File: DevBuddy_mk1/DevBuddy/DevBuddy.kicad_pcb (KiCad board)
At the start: 2 copper layers, 283 parts, among them J1 2171820001, J2 Conn_01x02_Socket, J3 Debug Conn, J4 UART_Conns, J5 PC30, J6 Conn_01x15_Pin, Q1 AO3415A, Q10 AO3415A, Q2 BC817, Q3 BC817, Q4 AO3415A, Q5 BC817, Q6 AO3415A, Q7 BC817, Q8 AO3415A, Q9 BC817, U1 RP2354B, U10 TPS62913, U11 TPS54331DDAR, U12 MCP4725xxx-xCH, U13 TPS55289RYQR, U14 MCP4725xxx-xCH, U15 NCP1117-3.3_SOT223, U16 74HC4051, U17 TPS22965NQWDSGRQ1, U18 TPS22965NQWDSGRQ1, U19 TPS22965NQWDSGRQ1, U2 74HC4051, U3 74HC4051, U4 INA190A2IDCKR, U5 TPS54331DDAR, U6 TPS54331DDAR, U7 TPS62913, U8 TPS62913, U9 TPS55289RYQR, Y1 12MHz

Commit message: PCB, initial routing of submods
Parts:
- R13, R14, R26, R27, R8, R9: footprint Resistor_SMD:R_01005_0402Metric -> Resistor_SMD:R_0402_1005Metric
- moved R46 241.5 mm to (23.4, 150.4)
- moved R35 239.7 mm to (23.4, 152.4), turned to 180 degrees
- moved R34 239.5 mm to (23.4, 149.4), turned to 180 degrees
- moved C85 237.5 mm to (23.4, 151.4), turned to 180 degrees
- moved U13 237.3 mm to (29.4, 149.4)
- moved R33 235.1 mm to (23.4, 148.4)
- moved R51 233.8 mm to (35.0, 154.7), turned to -90 degrees
- moved C83 233.4 mm to (28.2, 153.3)
- moved C93 233.0 mm to (32.6, 163.6), turned to 180 degrees
- moved R52 232.4 mm to (36.0, 154.7), turned to -90 degrees
- moved R48 231.9 mm to (36.9, 149.2), turned to 90 degrees
- moved R41 231.9 mm to (34.0, 149.2), turned to 90 degrees
- moved C81 229.2 mm to (25.1, 159.5)
- moved C87 228.6 mm to (35.4, 148.7), turned to 180 degrees
- moved C102 228.4 mm to (35.5, 153.2)
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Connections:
- R13 pad 1: Net-(U6-VSENSE) -> 12V_C_CurSense_Hi
- R13 pad 2: 12V_C_CurSense_Hi -> Net-(U6-VSENSE)
- R14 pad 1: GND -> Net-(U6-VSENSE)
- R14 pad 2: Net-(U6-VSENSE) -> GND
- R26 pad 1: Net-(U11-VSENSE) -> 12V_D_CurSense_Hi
- R26 pad 2: 12V_D_CurSense_Hi -> Net-(U11-VSENSE)
- R27 pad 1: GND -> Net-(U11-VSENSE)
- R27 pad 2: Net-(U11-VSENSE) -> GND
- R8 pad 1: Net-(U5-VSENSE) -> +3V3
- R8 pad 2: +3V3 -> Net-(U5-VSENSE)
- R9 pad 1: GND -> Net-(U5-VSENSE)
- R9 pad 2: Net-(U5-VSENSE) -> GND
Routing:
- net +3V3: track 0.00 -> 64.3 mm
- net 5V_D_CurSense_Hi: track 0.00 -> 38.3 mm
- net 5V_C_CurSense_Hi: track 0.00 -> 36.9 mm
- net 3V3_C_CurSense_Hi: track 0.00 -> 33.2 mm
- net 12V_C_CurSense_Hi: track 0.00 -> 25.0 mm
- net 12V_D_CurSense_Hi: track 0.00 -> 24.3 mm
- net /Power_Supply_2/VCC_buck: track 0.00 -> 22.5 mm, vias 0 -> 3
- net /Power_Supply_2/VCC_buck_2: track 0.00 -> 21.2 mm, vias 0 -> 2
- net Net-(U1-XIN): track 0.00 -> 16.4 mm
- net AGND: track 0.00 -> 14.6 mm
- net GND: track 0.00 -> 13.6 mm
- net /ADC_Channels/ADC_in_Hi: track 0.00 -> 11.6 mm
- net /ADC_Channels/ADC_in_Low: track 0.00 -> 10.8 mm
- net Net-(U5-BOOT): track 0.00 -> 8.64 mm, vias 0 -> 2
- net Net-(U6-BOOT): track 0.00 -> 8.60 mm, vias 0 -> 2
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- added copper zone on F.Cu, net +3V3
- added copper zone on F.Cu, net 12V_C_CurSense_Hi
- added copper zone on F.Cu, net 12V_C_CurSense_Low
- added copper zone on F.Cu, net 12V_D_CurSense_Hi
- added copper zone on F.Cu, net 12V_D_CurSense_Low
- added copper zone on F.Cu, net 3V3_C_CurSense_Hi
- added copper zone on F.Cu, net 3V3_C_CurSense_Low
- added copper zone on F.Cu, net 5V_C_CurSense_Hi
- added copper zone on F.Cu, net 5V_D_CurSense_Hi
- added copper zone on F.Cu, net GND
- added copper zone on F.Cu, net Net-(D1-K)
- added copper zone on F.Cu, net Net-(D2-K)
- added copper zone on F.Cu, net Net-(D3-K)
- added copper zone on F.Cu, net Net-(R43-Pad2)
- added copper zone on F.Cu, net Net-(R45-Pad2)
- added copper zone on F.Cu, net Net-(U10-VO)
- added copper zone on F.Cu, net Net-(U13-SW1)
- added copper zone on F.Cu, net Net-(U13-SW2)
- added copper zone on F.Cu, net Net-(U7-SW)
- added copper zone on F.Cu, net Net-(U7-VO)
- added copper zone on F.Cu, net Net-(U8-SW)
- added copper zone on F.Cu, net Net-(U8-VO)
- added copper zone on F.Cu, net Net-(U9-SW1)
- added copper zone on F.Cu, net Net-(U9-SW2)
- added copper zone on F.Cu, net VCC_CurSense_Low
- added copper zone on F.Cu, net Var_V1_CurSense_Hi
- added copper zone on F.Cu, net Var_V1_CurSense_Low
- added copper zone on F.Cu, net Var_V2_CurSense_Hi
- added copper zone on F.Cu, net Var_V2_CurSense_Low

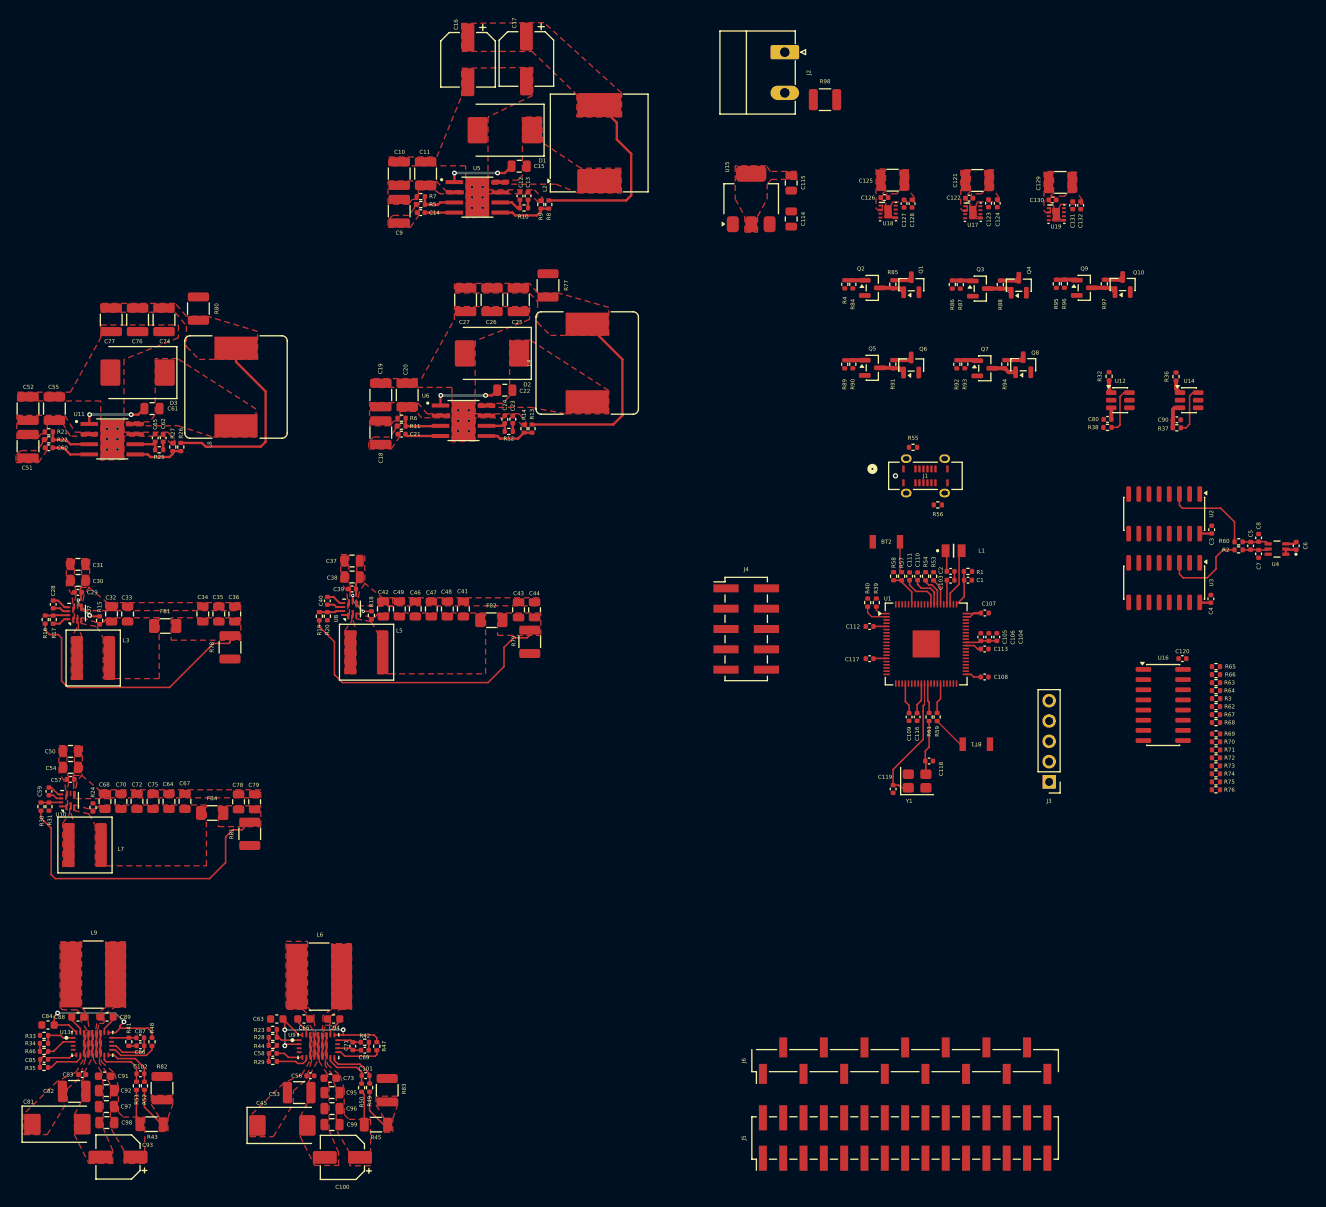
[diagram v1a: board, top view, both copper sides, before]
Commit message: PCB, first draft of PCB layout
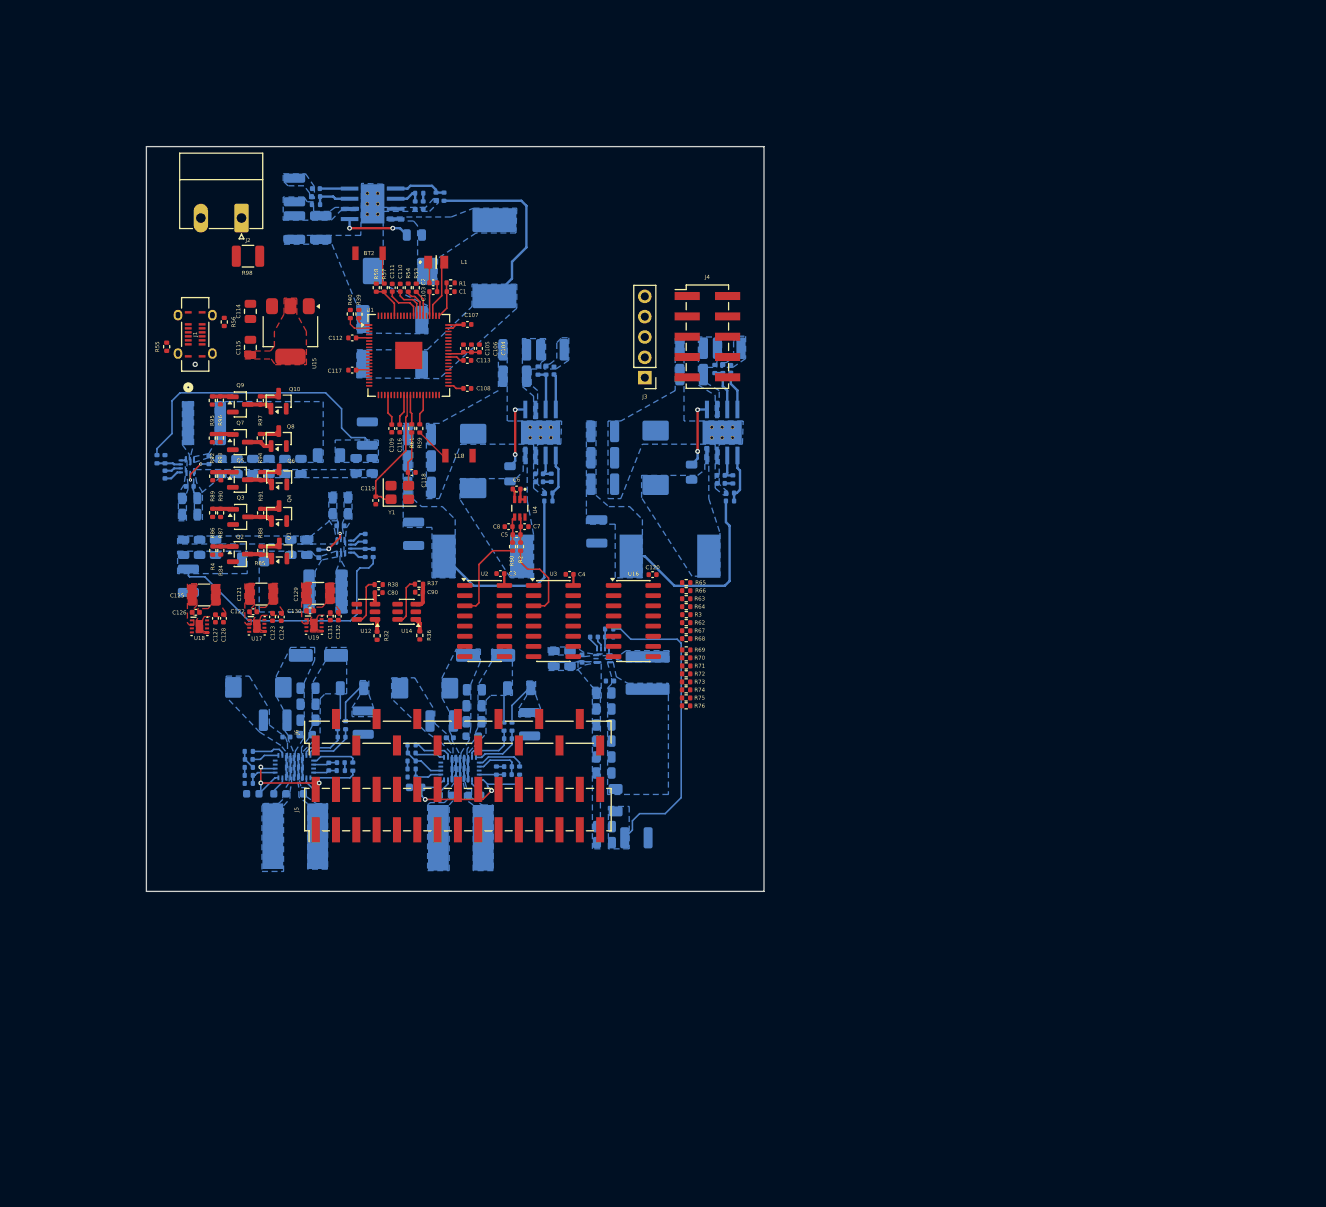
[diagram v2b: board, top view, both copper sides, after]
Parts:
- C10, C100, C101, C102, C11, C12, C13, C14, C15, C16, C17, C18, C19, C20, C21, C22, C23, C24, C25, C26, C27, C28, C29, C30, C31, C32, C33, C34, C35, C36, C37, C38, C39, C40, C41, C42, C43, C44, C45, C46, C47, C48, C49, C50, C51, C52, C53, C54, C55, C56, C57, C58, C59, C60, C61, C62, C63, C64, C65, C66, C67, C68, C69, C70, C71, C72, C73, C74, C75, C76, C77, C78, C79, C81, C82, C83, C84, C85, C86, C87, C88, C89, C9, C91, C92, C93, C94, C95, C96, C97, C98, C99, D1, D2, D3, FB1, FB2, FB4, L2, L3, L4, L5, L6, L7, L8, L9, R10, R11, R12, R13, R14, R15, R16, R17, R18, R19, R20, R21, R22, R23, R24, R25, R26, R27, R28, R29, R30, R31, R33, R34, R35, R41, R42, R43, R44, R45, R46, R47, R48, R49, R5, R50, R51, R52, R6, R7, R77, R78, R79, R8, R80, R81, R82, R83, R9, U10, U11, U13, U5, U6, U7, U8, U9: moved to B.Cu
- moved Q10 106.5 mm to (52.7, 69.1)
- moved Q9 106.5 mm to (47.9, 69.5)
- moved R95 106.5 mm to (44.4, 69.0)
- moved R96 106.5 mm to (45.4, 69.0)
- moved R97 106.5 mm to (50.4, 69.0)
- moved U19 106.1 mm to (57.2, 97.1)
- moved C129 106.1 mm to (57.7, 93.1)
- moved C130 106.1 mm to (56.7, 95.3)
- moved C131 106.1 mm to (59.2, 96.0)
- moved C132 106.1 mm to (60.2, 96.0)
- moved C121 103.4 mm to (50.6, 93.2)
- moved C123 103.4 mm to (52.0, 96.1)
- moved C124 103.4 mm to (53.1, 96.1)
- moved U17 103.4 mm to (50.0, 97.2)
- moved C122 103.4 mm to (49.5, 95.4)
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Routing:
- net 12V_C_CurSense_Hi: track 25.0 -> 24.1 mm
- added copper zone on B.Cu, net +3V3
- added copper zone on B.Cu, net 12V_C_CurSense_Hi
- added copper zone on B.Cu, net 12V_C_CurSense_Low
- added copper zone on B.Cu, net 12V_D_CurSense_Hi
- added copper zone on B.Cu, net 12V_D_CurSense_Low
- added copper zone on B.Cu, net 3V3_C_CurSense_Hi
- added copper zone on B.Cu, net 5V_C_CurSense_Hi
- added copper zone on B.Cu, net 5V_D_CurSense_Hi
- added copper zone on B.Cu, net GND
- added copper zone on B.Cu, net Net-(D1-K)
- added copper zone on B.Cu, net Net-(D2-K)
- added copper zone on B.Cu, net Net-(D3-K)
- added copper zone on B.Cu, net Net-(R43-Pad2)
- added copper zone on B.Cu, net Net-(R45-Pad2)
- added copper zone on B.Cu, net Net-(U10-VO)
- added copper zone on B.Cu, net Net-(U13-SW1)
- added copper zone on B.Cu, net Net-(U13-SW2)
- added copper zone on B.Cu, net Net-(U7-SW)
- added copper zone on B.Cu, net Net-(U7-VO)
- added copper zone on B.Cu, net Net-(U8-SW)
- added copper zone on B.Cu, net Net-(U8-VO)
- added copper zone on B.Cu, net Net-(U9-SW1)
- added copper zone on B.Cu, net Net-(U9-SW2)
- added copper zone on B.Cu, net VCC_CurSense_Low
- added copper zone on B.Cu, net Var_V1_CurSense_Hi
- added copper zone on B.Cu, net Var_V2_CurSense_Hi
- removed copper zone on F.Cu, net 12V_C_CurSense_Hi
- removed copper zone on F.Cu, net 12V_C_CurSense_Low
- removed copper zone on F.Cu, net 12V_D_CurSense_Hi
- removed copper zone on F.Cu, net 12V_D_CurSense_Low
- removed copper zone on F.Cu, net 3V3_C_CurSense_Hi
- removed copper zone on F.Cu, net 5V_C_CurSense_Hi
- removed copper zone on F.Cu, net 5V_D_CurSense_Hi
- removed copper zone on F.Cu, net Net-(D1-K)
- removed copper zone on F.Cu, net Net-(D2-K)
- removed copper zone on F.Cu, net Net-(D3-K)
- removed copper zone on F.Cu, net Net-(R43-Pad2)
- removed copper zone on F.Cu, net Net-(R45-Pad2)
- removed copper zone on F.Cu, net Net-(U10-VO)
- removed copper zone on F.Cu, net Net-(U13-SW1)
- removed copper zone on F.Cu, net Net-(U13-SW2)
- removed copper zone on F.Cu, net Net-(U7-SW)
- removed copper zone on F.Cu, net Net-(U7-VO)
- removed copper zone on F.Cu, net Net-(U8-SW)
- removed copper zone on F.Cu, net Net-(U8-VO)
- removed copper zone on F.Cu, net Net-(U9-SW1)
- removed copper zone on F.Cu, net Net-(U9-SW2)
- removed copper zone on F.Cu, net VCC_CurSense_Low
- removed copper zone on F.Cu, net Var_V1_CurSense_Hi
- removed copper zone on F.Cu, net Var_V2_CurSense_Hi
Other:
- board outline added: 77.2 x 93.1 mm
- copper layers 2 -> 4

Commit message: PCB, Progress in routing.
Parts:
- removed R55, R56: 5k1, Resistor_SMD:R_0402_1005Metric
- added C133: 100n, Capacitor_SMD:C_0402_1005Metric, F.Cu at (77.3, 60.6)
- added C134: 100n, Capacitor_SMD:C_0402_1005Metric, F.Cu at (65.9, 54.9)
- J1: value 2171820001 -> 10118194-0001LF; footprint USB-C_Vertical:CONN_2171820001_MOL -> usb_micro_b:AMPHENOL_10118194-0001LF
- J3: footprint Connector_PinHeader_2.54mm:PinHeader_1x05_P2.54mm_Vertical -> Connector_PinHeader_2.54mm:PinHeader_1x05_P2.54mm_Vertical_SMD_Pin1Left
- R98: moved to B.Cu
- moved J4 60.3 mm to (46.0, 63.4)
- moved J3 52.1 mm to (47.0, 74.0), turned to -90 degrees
- moved C4 50.2 mm to (137.5, 77.6)
- moved U3 50.2 mm to (135.5, 83.4)
- moved C5 49.5 mm to (130.4, 73.5)
- moved C6 49.5 mm to (130.4, 67.8)
- moved C7 49.5 mm to (131.4, 72.5)
- moved C8 49.5 mm to (129.4, 72.5)
- moved R2 49.5 mm to (130.9, 75.0)
- moved R60 49.5 mm to (129.9, 75.0)
- moved U4 49.5 mm to (130.8, 70.2)
- moved U2 48.7 mm to (125.3, 83.1)
- moved C3 48.7 mm to (127.3, 77.2)
- moved J1 43.0 mm to (79.2, 38.8), turned to 180 degrees
- moved R3 38.4 mm to (141.5, 102.3)
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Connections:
- net Net-(U1-USB_DM) renamed /DevBuddy_Logic/D-
- net Net-(U1-USB_DP) renamed /DevBuddy_Logic/D+
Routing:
- net GND: track 13.6 -> 172.0 mm, vias 0 -> 72
- net VCC_CurSense_Low: track 2.43 -> 57.8 mm
- net 12V_C_CurSense_Low: track 3.16 -> 58.2 mm
- net 3V3_C_CurSense_Low: track 0.00 -> 53.7 mm
- net /DevBuddy_Logic/UART_RX_MCU: track 0.00 -> 48.6 mm
- net 5V_D_CurSense_Low: track 2.46 -> 50.3 mm
- net /DevBuddy_Logic/UART_TX_MCU: track 0.00 -> 45.8 mm
- net VarBuck1_DAC_out: track 0.00 -> 45.1 mm
- net +12VDC_C_Out: track 0.00 -> 44.8 mm
- net 5V_C_CurSense_Low: track 2.47 -> 45.1 mm
- net +5V_D_Out: track 0.00 -> 39.5 mm
- net Var_V2_CurSense_Low: track 0.00 -> 39.4 mm
- net 12V_D_CurSense_Low: track 3.18 -> 41.7 mm
- net VarBuck2_DAC_out: track 0.00 -> 35.8 mm
- net +5V_C_Out: track 0.00 -> 33.2 mm
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- added copper zone on F.Cu, net +3V3_C_Out
- added copper zone on F.Cu, net +Var_V_1_Out
- added copper zone on F.Cu, net +Var_V_2_Out
- added copper zone on In1.Cu, net GND
- added copper zone on B.Cu, net VCC_CurSense_Hi

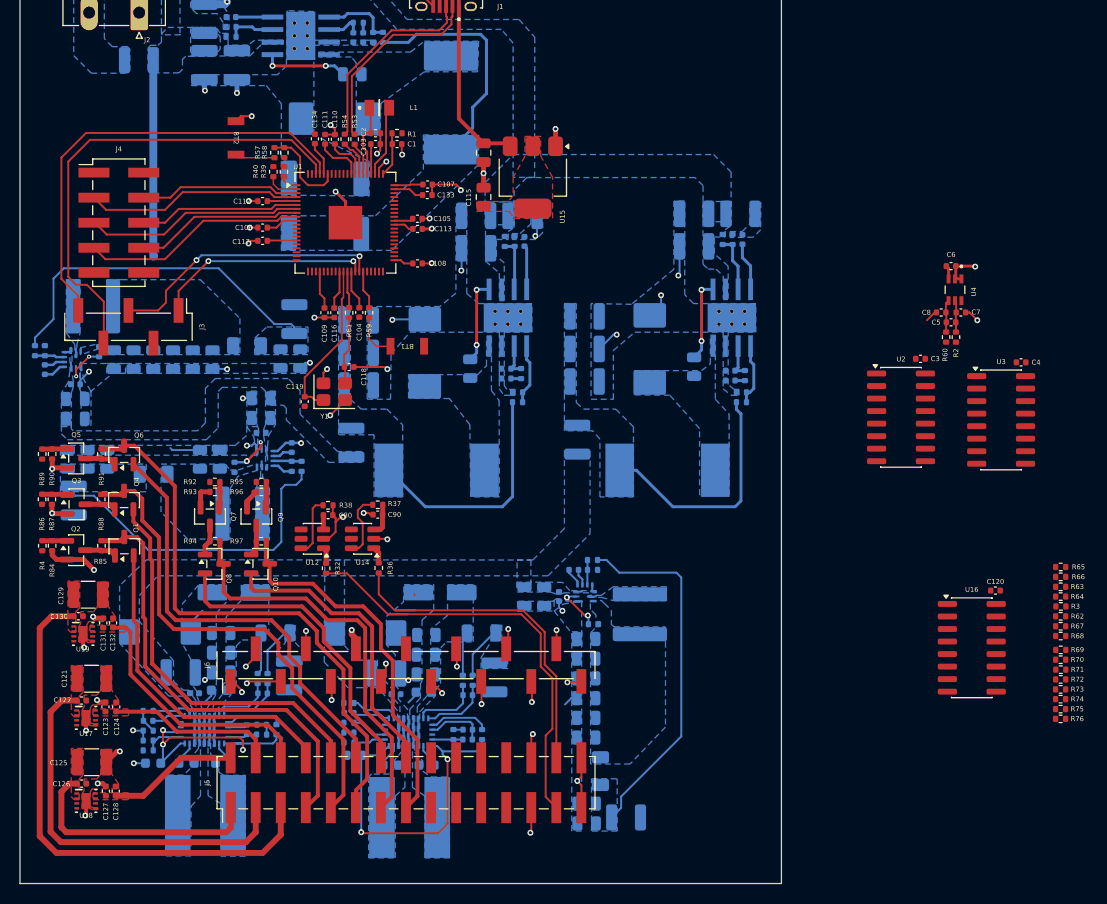
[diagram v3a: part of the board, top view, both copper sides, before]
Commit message: PCB, Power routing nearly complete.
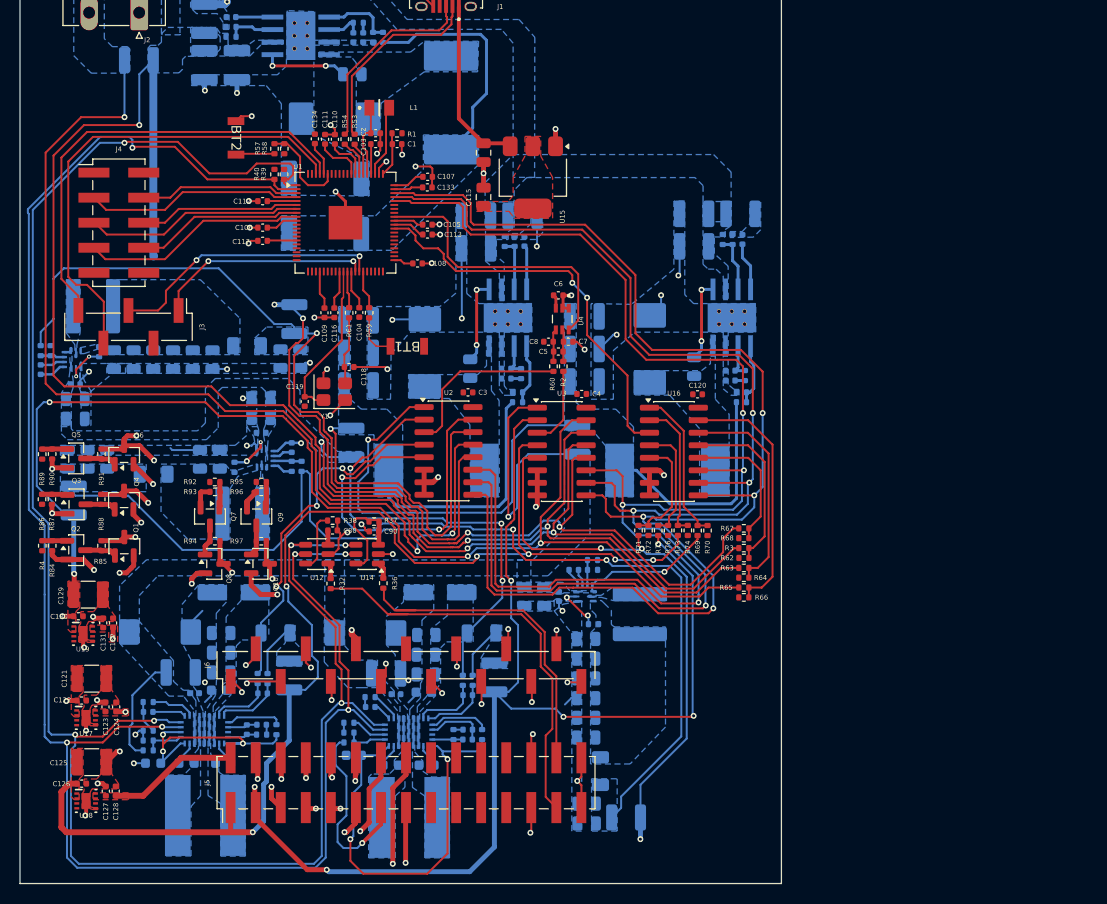
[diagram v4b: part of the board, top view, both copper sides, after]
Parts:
- moved C3 46.0 mm to (81.4, 80.6)
- moved U2 46.0 mm to (79.5, 86.5)
- moved R71 45.1 mm to (98.7, 94.6), turned to -90 degrees
- moved C4 44.7 mm to (93.0, 80.8)
- moved U3 44.7 mm to (90.9, 86.6)
- moved R75 44.6 mm to (100.7, 94.6), turned to -90 degrees
- moved R72 44.4 mm to (99.7, 94.6), turned to 90 degrees
- moved R76 44.1 mm to (101.7, 94.6), turned to 90 degrees
- moved R73 42.0 mm to (102.7, 94.6), turned to -90 degrees
- moved R74 41.5 mm to (103.7, 94.6), turned to 90 degrees
- moved C5 39.9 mm to (90.6, 76.5)
- moved C6 39.9 mm to (90.6, 70.8)
- moved C7 39.9 mm to (91.6, 75.5)
- moved C8 39.9 mm to (89.6, 75.5)
- moved R2 39.9 mm to (91.1, 78.0)
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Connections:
- R19 pad 2: /Power_Supply_1/buck_fb -> /Power_Supply_1/buck_fb1
- R20 pad 1: /Power_Supply_1/buck_fb -> /Power_Supply_1/buck_fb1
- R30 pad 2: /Power_Supply_1/buck_fb -> /Power_Supply_1/buck_fb2
- R31 pad 1: /Power_Supply_1/buck_fb -> /Power_Supply_1/buck_fb2
- U1 pad 18: MUX_S0 -> unconnected-(U1-GPIO18-Pad18)
- U1 pad 19: MUX_S1 -> unconnected-(U1-GPIO19-Pad19)
- U1 pad 20: MUX_S2 -> unconnected-(U1-GPIO20-Pad20)
- U1 pad 56: unconnected-(U1-GPIO45/ADC5-Pad56) -> MUX_S0
- U1 pad 57: unconnected-(U1-GPIO46/ADC6-Pad57) -> MUX_S1
- U1 pad 58: unconnected-(U1-GPIO47/ADC7-Pad58) -> MUX_S2
- U10 pad 9: /Power_Supply_1/buck_fb -> /Power_Supply_1/buck_fb2
- U8 pad 9: /Power_Supply_1/buck_fb -> /Power_Supply_1/buck_fb1
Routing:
- net I2C_SDA: track 1.89 -> 189.5 mm, vias 0 -> 6
- net I2C_SCL: track 3.32 -> 188.0 mm, vias 0 -> 6
- net VCC_CurSense_Low: track 57.8 -> 208.2 mm, vias 0 -> 5
- net MUX_S2: track 0.00 -> 137.2 mm, vias 0 -> 4
- net MUX_S1: track 0.00 -> 136.0 mm, vias 0 -> 4
- net MUX_S0: track 0.00 -> 134.9 mm, vias 0 -> 4
- net 5V_C_CurSense_Low: track 45.1 -> 167.0 mm, vias 0 -> 6
- net Var_V2_CurSense_Low: track 39.4 -> 145.2 mm, vias 0 -> 7
- net VCC_CurSense_Hi: track 0.00 -> 102.8 mm, vias 0 -> 3
- net 3V3_C_CurSense_Low: track 53.7 -> 154.0 mm, vias 0 -> 6
- net Var_V1_CurSense_Low: track 25.1 -> 122.2 mm, vias 0 -> 6
- net 5V_D_CurSense_Low: track 50.3 -> 145.2 mm, vias 0 -> 5
- net 12V_C_CurSense_Low: track 58.2 -> 135.5 mm, vias 0 -> 6
- net 12V_D_CurSense_Low: track 41.7 -> 112.8 mm, vias 0 -> 4
- net 5V_C_CurSense_Hi: track 35.5 -> 82.1 mm, vias 0 -> 1
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- added copper zone on B.Cu, net Net-(U10-SW)
